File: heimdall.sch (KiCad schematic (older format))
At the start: 20 parts, among them P1 CONN, Q1 FDN337N, U1 ESP-01, U2 TLP222A, U3 TPS62177

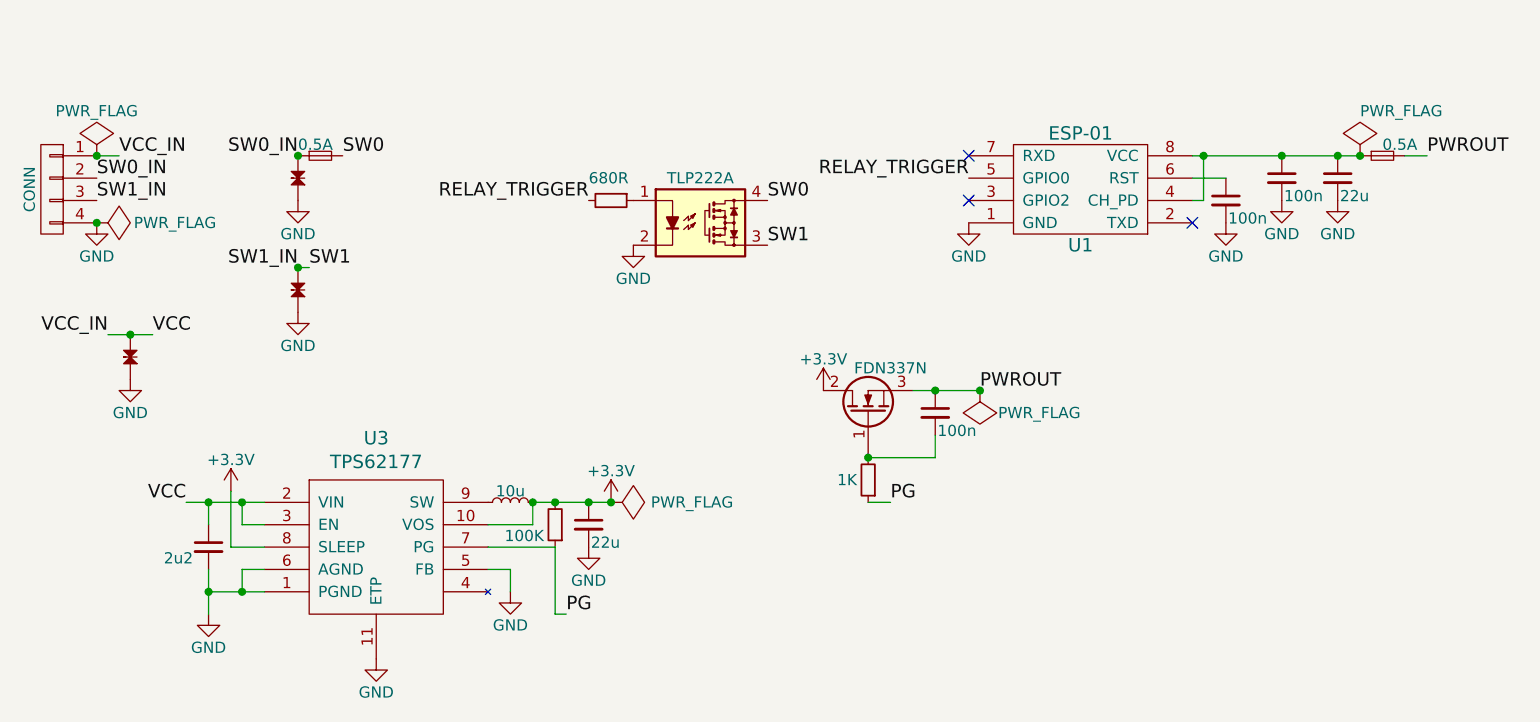
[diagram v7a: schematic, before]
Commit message: Comments based on davids advice
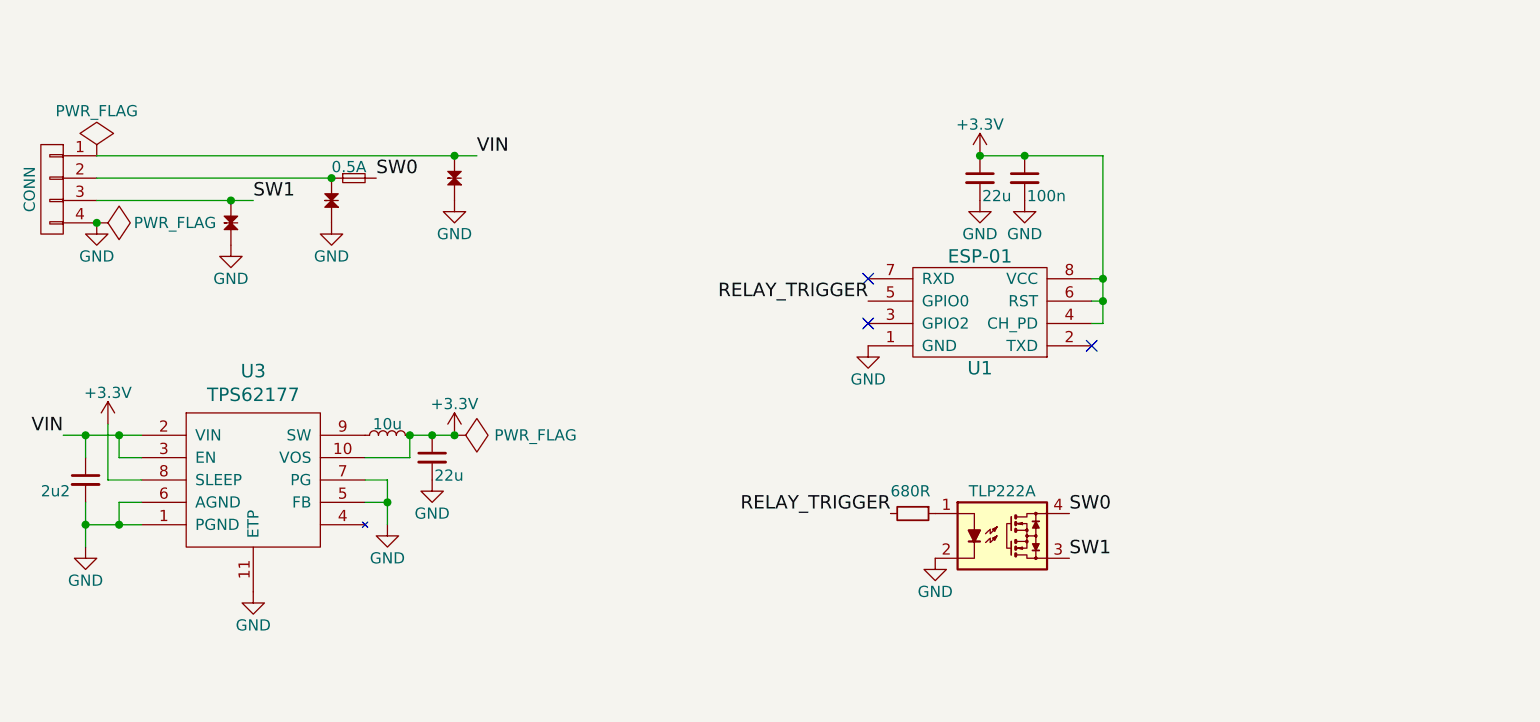
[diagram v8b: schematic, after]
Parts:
- removed C2, C3: 100n, Capacitors_SMD:C_0603, symbol C_Small
- removed F2: 0.5A, Resistors_SMD:R_1206, symbol F_Small
- removed Q1: FDN337N, Housings_SSOT:SuperSOT-3, symbol Q_NMOS_GDS
- removed R2: 100K, Resistors_SMD:R_0603, symbol R_Small
- removed R3: 1K, Resistors_SMD:R_0603, symbol R_Small
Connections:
- net PG is gone; now on net GND: U3.7 (PG)
- net +3V3: now also C4.1, C5.1, U1.4 (CH_PD), U1.6 (RST), U1.8 (VCC)
- net SW0_IN: no longer names the net of D3.1 (K), F1.1, P1.2 (P2)
- net VCC renamed VIN
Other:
- moved on the sheet: U1, U3
